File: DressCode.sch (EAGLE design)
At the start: 41 parts, among them M1 MIC9.7MM, M2 MIC6MM, Q1 2N7002, Q2 2N7002, Q3 2N7002, U1 MCP6S21, U2 MCP6S21, U3 MCP6G02, U4 PIC24FV32KA304-I/PT, U5 MCP73832T-2ACI/OT

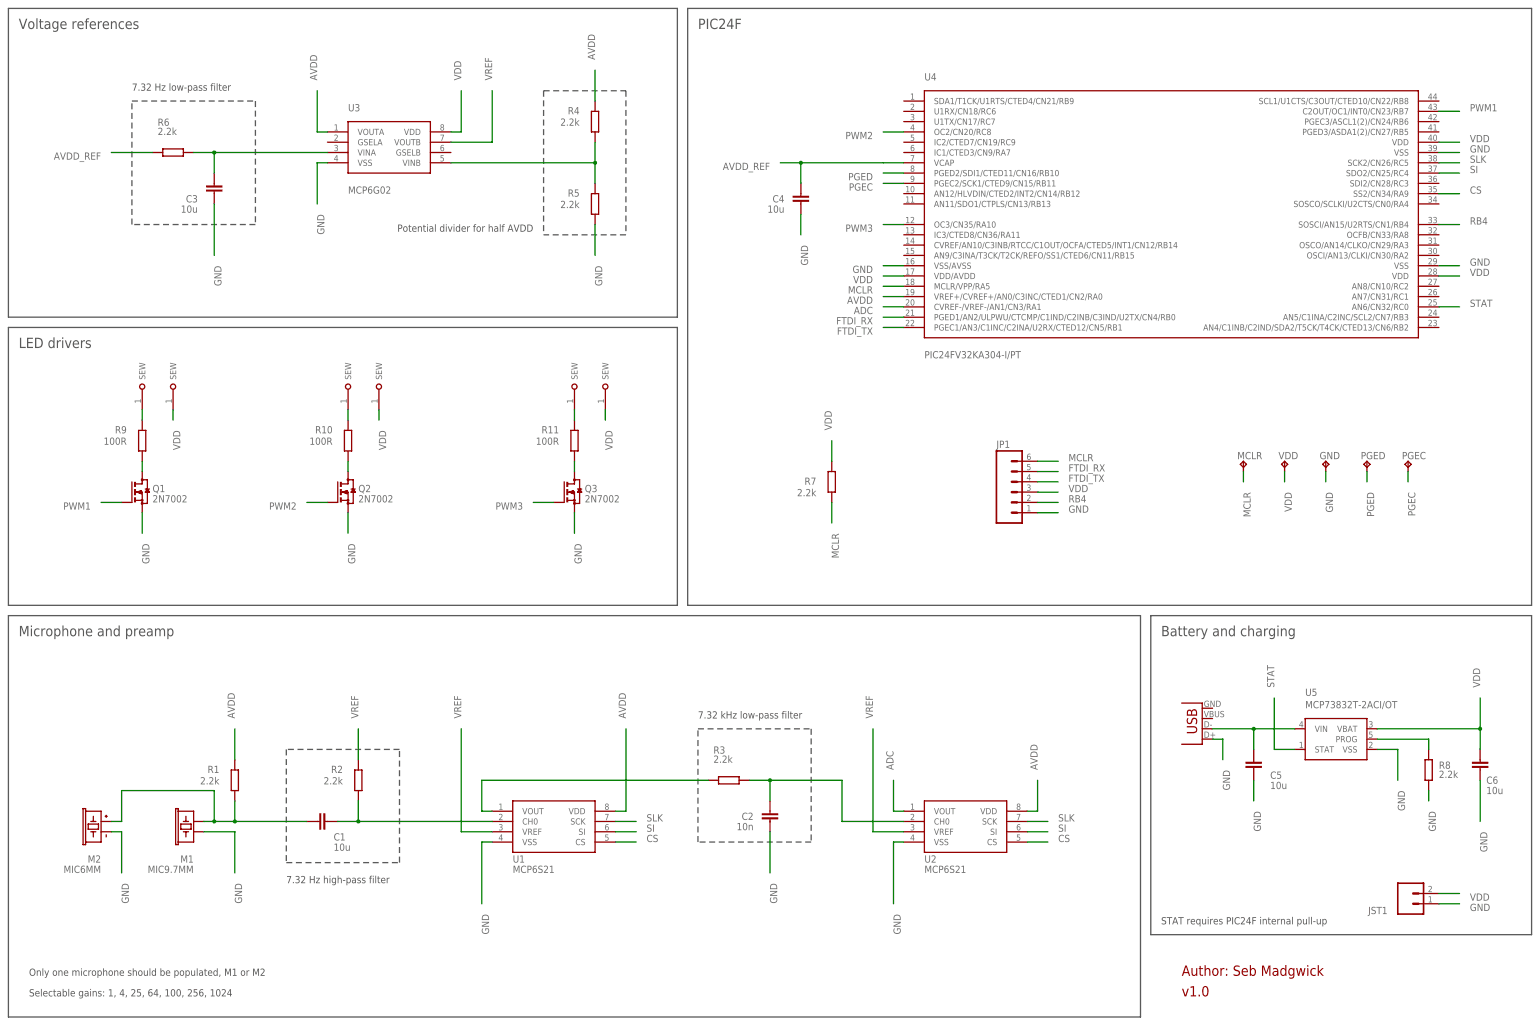
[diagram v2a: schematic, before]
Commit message: added power switch
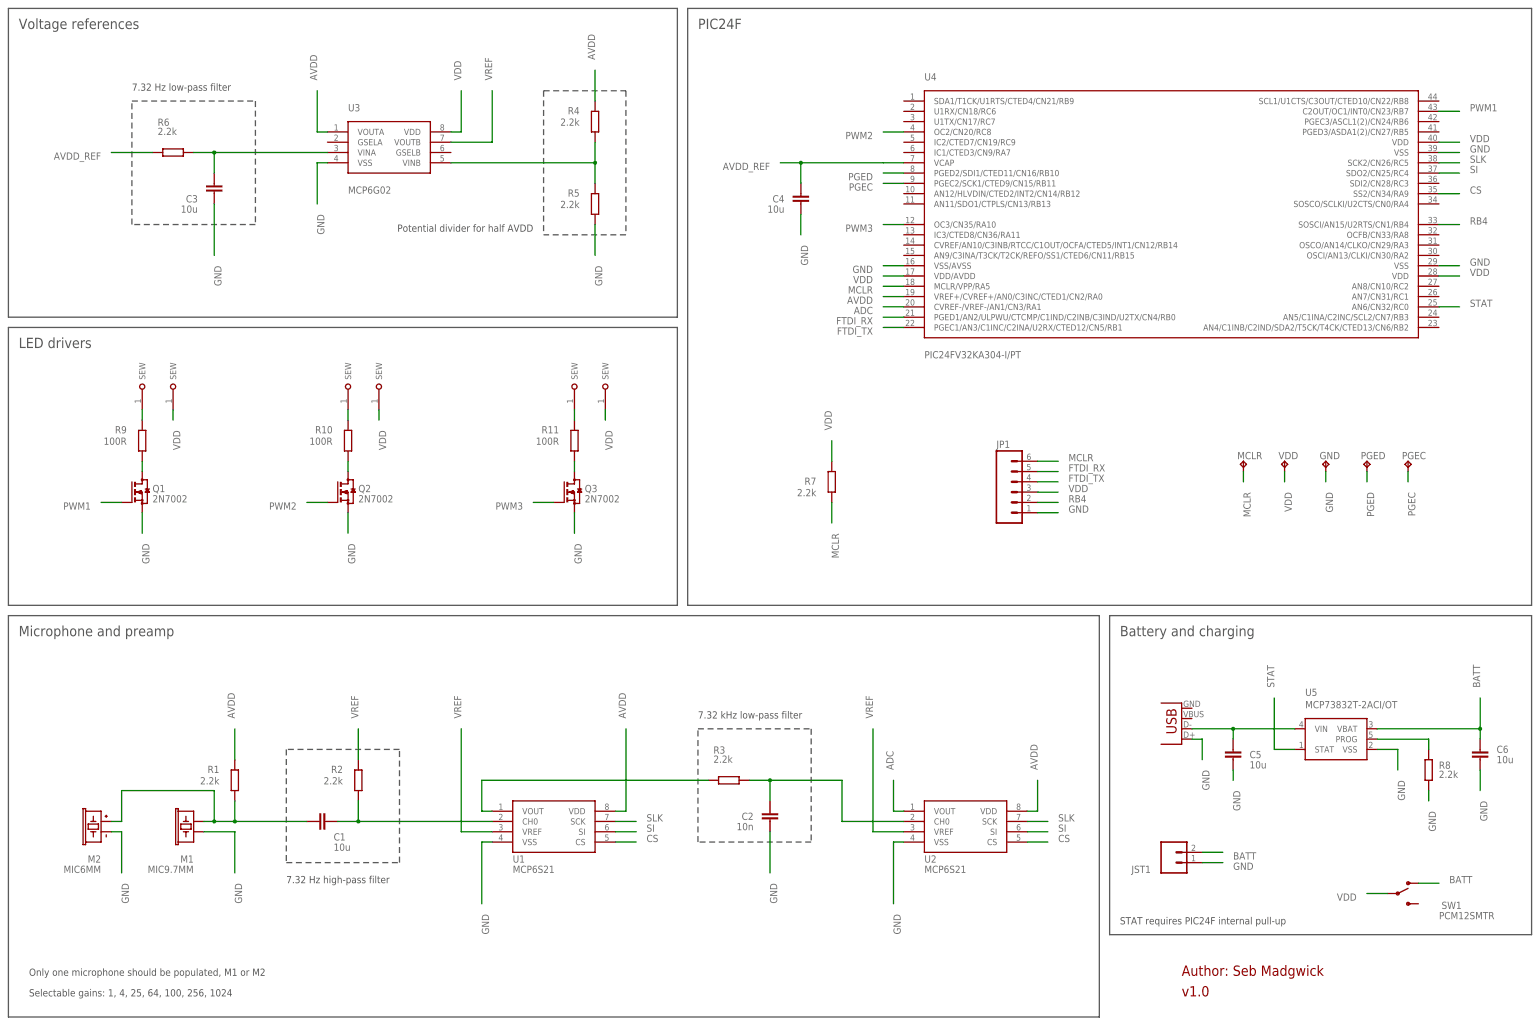
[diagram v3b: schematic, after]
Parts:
- added SW1: PCM12SMTR, SparkFun0modified:PCM12SMTR
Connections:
- new net BATT: C6.2, JST1.2, SW1.O, U5.VBAT
- net VDD: now also SW1.P; no longer C6.2, JST1.2, U5.VBAT
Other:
- moved on the sheet: C5, C6, JST1
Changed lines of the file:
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@@
 <part name="U$8" library="x-io" deviceset="DRESSCODE_SEW_PAD" device="S"/>
 <part name="U$10" library="x-io" deviceset="DRESSCODE_SEW_PAD" device="S"/>
+<part name="SW1" library="SparkFun0modified" deviceset="PCM12SMTR" device=""/>
 </parts>
 <sheets>
@@
 <wire x1="203.2" y1="48.26" x2="175.26" y2="48.26" width="0.1524" layer="97" style="shortdash"/>
 <wire x1="175.26" y1="48.26" x2="175.26" y2="76.2" width="0.1524" layer="97" style="shortdash"/>
-<wire x1="5.08" y1="104.14" x2="284.48" y2="104.14" width="0.1524" layer="97"/>
-<wire x1="284.48" y1="104.14" x2="284.48" y2="5.08" width="0.1524" layer="97"/>
-<wire x1="284.48" y1="5.08" x2="5.08" y2="5.08" width="0.1524" layer="97"/>
+<wire x1="5.08" y1="104.14" x2="274.32" y2="104.14" width="0.1524" layer="97"/>
+<wire x1="274.32" y1="104.14" x2="274.32" y2="5.08" width="0.1524" layer="97"/>
+<wire x1="274.32" y1="5.08" x2="5.08" y2="5.08" width="0.1524" layer="97"/>
 <wire x1="5.08" y1="5.08" x2="5.08" y2="104.14" width="0.1524" layer="97"/>
 <wire x1="5.08" y1="254" x2="170.18" y2="254" width="0.1524" layer="97"/>
@@
 <wire x1="381" y1="106.68" x2="172.72" y2="106.68" width="0.1524" layer="97"/>
 <wire x1="172.72" y1="106.68" x2="172.72" y2="254" width="0.1524" layer="97"/>
-<wire x1="287.02" y1="104.14" x2="381" y2="104.14" width="0.1524" layer="97"/>
+<wire x1="276.86" y1="104.14" x2="381" y2="104.14" width="0.1524" layer="97"/>
 <wire x1="381" y1="104.14" x2="381" y2="25.4" width="0.1524" layer="97"/>
-<wire x1="381" y1="25.4" x2="287.02" y2="25.4" width="0.1524" layer="97"/>
-<wire x1="287.02" y1="25.4" x2="287.02" y2="104.14" width="0.1524" layer="97"/>
+<wire x1="381" y1="25.4" x2="276.86" y2="25.4" width="0.1524" layer="97"/>
+<wire x1="276.86" y1="25.4" x2="276.86" y2="104.14" width="0.1524" layer="97"/>
 <text x="175.26" y="78.74" size="1.778" layer="97">7.32 kHz low-pass filter</text>
 <text x="73.66" y="38.1" size="1.778" layer="97">7.32 Hz high-pass filter</text>
@@
 <text x="7.62" y="170.18" size="2.54" layer="97">LED drivers</text>
 <text x="175.26" y="248.92" size="2.54" layer="97">PIC24F</text>
-<text x="289.56" y="99.06" size="2.54" layer="97">Battery and charging</text>
+<text x="279.4" y="99.06" size="2.54" layer="97">Battery and charging</text>
 <text x="294.64" y="15.24" size="2.54" layer="94">Author: Seb Madgwick</text>
 <text x="10.16" y="15.24" size="1.778" layer="97">Only one microphone should be populated, M1 or M2</text>
 <text x="294.64" y="10.16" size="2.54" layer="94">v1.0</text>
-<text x="289.56" y="27.94" size="1.778" layer="97">STAT requires PIC24F internal pull-up</text>
+<text x="279.4" y="27.94" size="1.778" layer="97">STAT requires PIC24F internal pull-up</text>
 </plain>
 <instances>
@@
 <attribute name="VALUE" x="325.12" y="81.28" size="1.778" layer="96"/>
 </instance>
-<instance part="USB1" gate="G$1" x="299.72" y="81.28" rot="R180"/>
-<instance part="C5" gate="G$1" x="312.42" y="66.04" smashed="yes" rot="R180">
-<attribute name="NAME" x="316.484" y="63.881" size="1.778" layer="95"/>
-<attribute name="VALUE" x="316.484" y="61.341" size="1.778" layer="96"/>
+<instance part="USB1" gate="G$1" x="294.64" y="81.28" rot="R180"/>
+<instance part="C5" gate="G$1" x="307.34" y="68.58" smashed="yes" rot="R180">
+<attribute name="NAME" x="311.404" y="68.961" size="1.778" layer="95"/>
+<attribute name="VALUE" x="311.404" y="66.421" size="1.778" layer="96"/>
 </instance>
 <instance part="R8" gate="G$1" x="355.6" y="66.04" smashed="yes" rot="R90">
@@
 <attribute name="VALUE" x="358.1146" y="64.0842" size="1.778" layer="96"/>
 </instance>
-<instance part="C6" gate="G$1" x="368.3" y="66.04" smashed="yes" rot="R180">
-<attribute name="NAME" x="369.824" y="62.6364" size="1.778" layer="95"/>
-<attribute name="VALUE" x="369.824" y="60.0964" size="1.778" layer="96"/>
-</instance>
-<instance part="JST1" gate="G$1" x="350.52" y="33.02" smashed="yes">
-<attribute name="VALUE" x="347.98" y="27.94" size="1.778" layer="96"/>
-<attribute name="NAME" x="345.44" y="32.258" size="1.778" layer="95" rot="R180"/>
+<instance part="C6" gate="G$1" x="368.3" y="68.58" smashed="yes" rot="R180">
+<attribute name="NAME" x="372.364" y="70.2564" size="1.778" layer="95"/>
+<attribute name="VALUE" x="372.364" y="67.7164" size="1.778" layer="96"/>
+</instance>
+<instance part="JST1" gate="G$1" x="292.1" y="43.18" smashed="yes">
+<attribute name="VALUE" x="289.56" y="38.1" size="1.778" layer="96"/>
+<attribute name="NAME" x="287.02" y="42.418" size="1.778" layer="95" rot="R180"/>
 </instance>
 <instance part="U$7" gate="G$1" x="38.1" y="160.02" rot="R90"/>
 <instance part="U$8" gate="G$1" x="88.9" y="160.02" rot="R90"/>
 <instance part="U$10" gate="G$1" x="144.78" y="160.02" rot="R90"/>
+<instance part="SW1" gate="G$1" x="347.98" y="35.56" smashed="yes">
+<attribute name="NAME" x="358.775" y="31.75" size="1.778" layer="95"/>
+<attribute name="VALUE" x="358.14" y="29.21" size="1.778" layer="96"/>
+</instance>
 </instances>
 <busses>
@@
 <segment>
 <pinref part="USB1" gate="G$1" pin="D+"/>
-<wire x1="302.26" y1="73.66" x2="304.8" y2="73.66" width="0.1524" layer="91"/>
-<wire x1="304.8" y1="73.66" x2="304.8" y2="68.58" width="0.1524" layer="91"/>
-<label x="304.8" y="66.04" size="1.778" layer="95" rot="R270"/>
+<wire x1="297.18" y1="73.66" x2="299.72" y2="73.66" width="0.1524" layer="91"/>
+<wire x1="299.72" y1="73.66" x2="299.72" y2="68.58" width="0.1524" layer="91"/>
+<label x="299.72" y="66.04" size="1.778" layer="95" rot="R270"/>
 </segment>
 <segment>
 <pinref part="C5" gate="G$1" pin="1"/>
-<wire x1="312.42" y1="63.5" x2="312.42" y2="58.42" width="0.1524" layer="91"/>
-<label x="312.42" y="55.88" size="1.778" layer="95" rot="R270"/>
+<wire x1="307.34" y1="66.04" x2="307.34" y2="63.5" width="0.1524" layer="91"/>
+<label x="307.34" y="60.96" size="1.778" layer="95" rot="R270"/>
 </segment>
 <segment>
 <pinref part="U5" gate="G$1" pin="VSS"/>
 <wire x1="342.9" y1="71.12" x2="347.98" y2="71.12" width="0.1524" layer="91"/>
-<wire x1="347.98" y1="71.12" x2="347.98" y2="63.5" width="0.1524" layer="91"/>
-<label x="347.98" y="60.96" size="1.778" layer="95" rot="R270"/>
+<wire x1="347.98" y1="71.12" x2="347.98" y2="66.04" width="0.1524" layer="91"/>
+<label x="347.98" y="63.5" size="1.778" layer="95" rot="R270"/>
 </segment>
 <segment>
@@
 <segment>
 <pinref part="C6" gate="G$1" pin="1"/>
-<wire x1="368.3" y1="63.5" x2="368.3" y2="53.34" width="0.1524" layer="91"/>
-<label x="368.3" y="50.8" size="1.778" layer="95" rot="R270"/>
+<wire x1="368.3" y1="66.04" x2="368.3" y2="60.96" width="0.1524" layer="91"/>
+<label x="368.3" y="58.42" size="1.778" layer="95" rot="R270"/>
 </segment>
 <segment>
 <pinref part="JST1" gate="G$1" pin="1"/>
-<wire x1="358.14" y1="33.02" x2="363.22" y2="33.02" width="0.1524" layer="91"/>
-<label x="365.76" y="33.02" size="1.778" layer="95" rot="MR180"/>
+<wire x1="299.72" y1="43.18" x2="304.8" y2="43.18" width="0.1524" layer="91"/>
+<label x="307.34" y="43.18" size="1.778" layer="95" rot="MR180"/>
 </segment>
 </net>
@@
 </segment>
 <segment>
-<pinref part="U5" gate="G$1" pin="VBAT"/>
-<wire x1="342.9" y1="76.2" x2="368.3" y2="76.2" width="0.1524" layer="91"/>
-<pinref part="C6" gate="G$1" pin="2"/>
-<wire x1="368.3" y1="71.12" x2="368.3" y2="76.2" width="0.1524" layer="91"/>
-<junction x="368.3" y="76.2"/>
-<wire x1="368.3" y1="76.2" x2="368.3" y2="83.82" width="0.1524" layer="91"/>
-<label x="368.3" y="86.36" size="1.778" layer="95" rot="R90"/>
-</segment>
-<segment>
-<pinref part="JST1" gate="G$1" pin="2"/>
-<wire x1="358.14" y1="35.56" x2="363.22" y2="35.56" width="0.1524" layer="91"/>
-<label x="365.76" y="35.56" size="1.778" layer="95" rot="MR180"/>
+<pinref part="SW1" gate="G$1" pin="P"/>
+<wire x1="345.44" y1="35.56" x2="340.36" y2="35.56" width="0.1524" layer="91"/>
+<label x="337.82" y="35.56" size="1.778" layer="95" rot="R180"/>
 </segment>
 </net>
@@
 <pinref part="USB1" gate="G$1" pin="D-"/>
 <pinref part="U5" gate="G$1" pin="VIN"/>
-<wire x1="302.26" y1="76.2" x2="312.42" y2="76.2" width="0.1524" layer="91"/>
+<wire x1="297.18" y1="76.2" x2="307.34" y2="76.2" width="0.1524" layer="91"/>
 <pinref part="C5" gate="G$1" pin="2"/>
-<wire x1="312.42" y1="76.2" x2="322.58" y2="76.2" width="0.1524" layer="91"/>
-<wire x1="312.42" y1="71.12" x2="312.42" y2="76.2" width="0.1524" layer="91"/>
-<junction x="312.42" y="76.2"/>
+<wire x1="307.34" y1="76.2" x2="322.58" y2="76.2" width="0.1524" layer="91"/>
+<wire x1="307.34" y1="73.66" x2="307.34" y2="76.2" width="0.1524" layer="91"/>
+<junction x="307.34" y="76.2"/>
 </segment>
 </net>
@@
 </segment>
 </net>
+<net name="BATT" class="0">
+<segment>
+<pinref part="JST1" gate="G$1" pin="2"/>
+<wire x1="299.72" y1="45.72" x2="304.8" y2="45.72" width="0.1524" layer="91"/>
+<label x="307.34" y="45.72" size="1.778" layer="95" rot="MR180"/>
+</segment>
+<segment>
+<pinref part="U5" gate="G$1" pin="VBAT"/>
+<wire x1="342.9" y1="76.2" x2="368.3" y2="76.2" width="0.1524" layer="91"/>
+<pinref part="C6" gate="G$1" pin="2"/>
+<wire x1="368.3" y1="73.66" x2="368.3" y2="76.2" width="0.1524" layer="91"/>
+<junction x="368.3" y="76.2"/>
+<wire x1="368.3" y1="76.2" x2="368.3" y2="83.82" width="0.1524" layer="91"/>
+<label x="368.3" y="86.36" size="1.778" layer="95" rot="R90"/>
+</segment>
+<segment>
+<pinref part="SW1" gate="G$1" pin="O"/>
+<wire x1="353.06" y1="38.1" x2="358.14" y2="38.1" width="0.1524" layer="91"/>
+<label x="360.68" y="38.1" size="1.778" layer="95"/>
+</segment>
+</net>

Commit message: Fix USB connection error
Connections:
- net GND: now also USB1.GND; no longer USB1.D+
- net USB1: now also USB1.VBUS; no longer USB1.D-
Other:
- note added: "v1.1"
- note removed: "v1.0"
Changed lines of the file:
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@@
 <text x="294.64" y="15.24" size="2.54" layer="94">Author: Seb Madgwick</text>
 <text x="10.16" y="15.24" size="1.778" layer="97">Only one microphone should be populated, M1 or M2</text>
-<text x="294.64" y="10.16" size="2.54" layer="94">v1.0</text>
+<text x="294.64" y="10.16" size="2.54" layer="94">v1.1</text>
 <text x="279.4" y="27.94" size="1.778" layer="97">STAT requires PIC24F internal pull-up</text>
 </plain>
@@
 <attribute name="VALUE" x="325.12" y="81.28" size="1.778" layer="96"/>
 </instance>
-<instance part="USB1" gate="G$1" x="294.64" y="81.28" rot="R180"/>
+<instance part="USB1" gate="G$1" x="294.64" y="73.66" rot="MR0"/>
 <instance part="C5" gate="G$1" x="307.34" y="68.58" smashed="yes" rot="R180">
 <attribute name="NAME" x="311.404" y="68.961" size="1.778" layer="95"/>
@@
 </segment>
 <segment>
-<pinref part="USB1" gate="G$1" pin="D+"/>
-<wire x1="297.18" y1="73.66" x2="299.72" y2="73.66" width="0.1524" layer="91"/>
 <wire x1="299.72" y1="73.66" x2="299.72" y2="68.58" width="0.1524" layer="91"/>
 <label x="299.72" y="66.04" size="1.778" layer="95" rot="R270"/>
+<pinref part="USB1" gate="G$1" pin="GND"/>
+<wire x1="297.18" y1="73.66" x2="299.72" y2="73.66" width="0.1524" layer="91"/>
 </segment>
 <segment>
@@
 <net name="USB1" class="0">
 <segment>
-<pinref part="USB1" gate="G$1" pin="D-"/>
 <pinref part="U5" gate="G$1" pin="VIN"/>
-<wire x1="297.18" y1="76.2" x2="307.34" y2="76.2" width="0.1524" layer="91"/>
 <pinref part="C5" gate="G$1" pin="2"/>
 <wire x1="307.34" y1="76.2" x2="322.58" y2="76.2" width="0.1524" layer="91"/>
 <wire x1="307.34" y1="73.66" x2="307.34" y2="76.2" width="0.1524" layer="91"/>
+<pinref part="USB1" gate="G$1" pin="VBUS"/>
+<wire x1="297.18" y1="76.2" x2="307.34" y2="76.2" width="0.1524" layer="91"/>
 <junction x="307.34" y="76.2"/>
 </segment>
